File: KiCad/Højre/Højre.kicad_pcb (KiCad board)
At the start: 2 copper layers, 14 parts, among them Q2 NMOS_IRL530, Q4 NMOS_IRL530, Q6 NMOS_IRL530

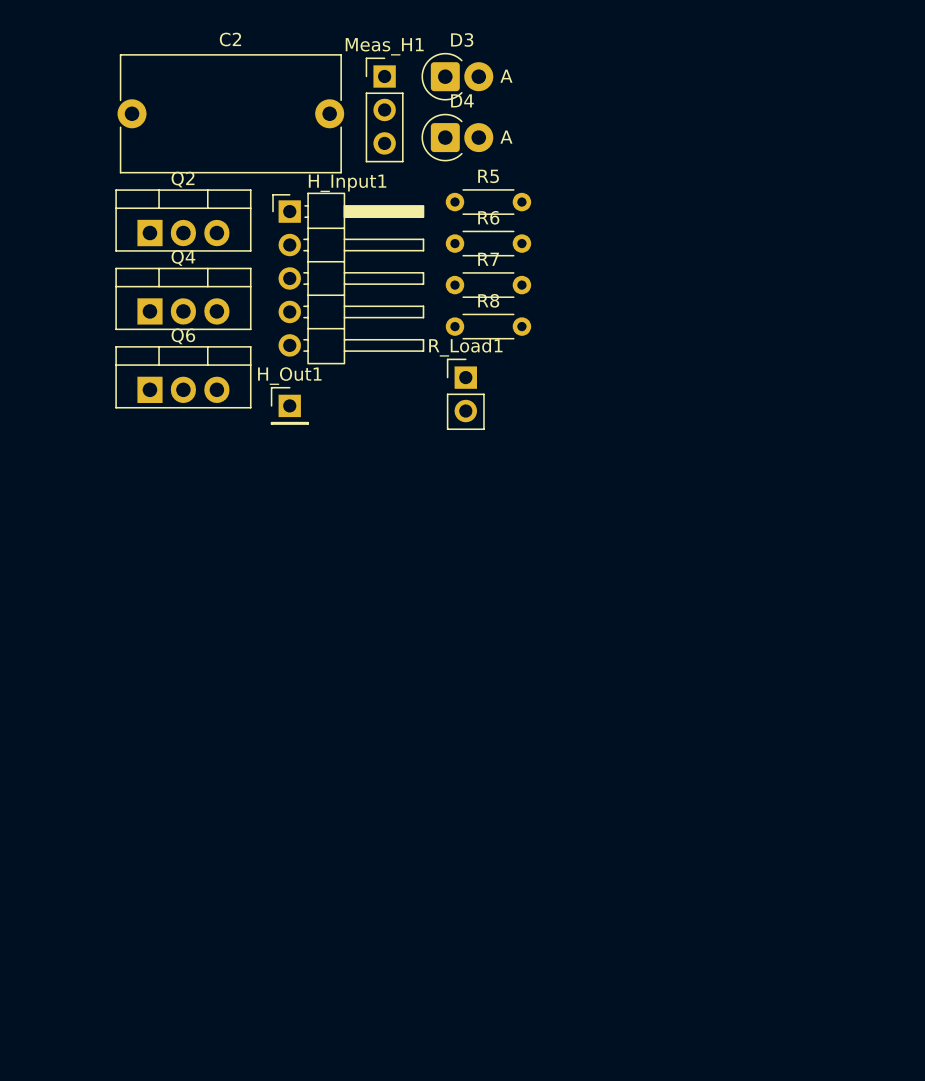
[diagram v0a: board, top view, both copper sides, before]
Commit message: Venstre og Højre pcb klar til produktion
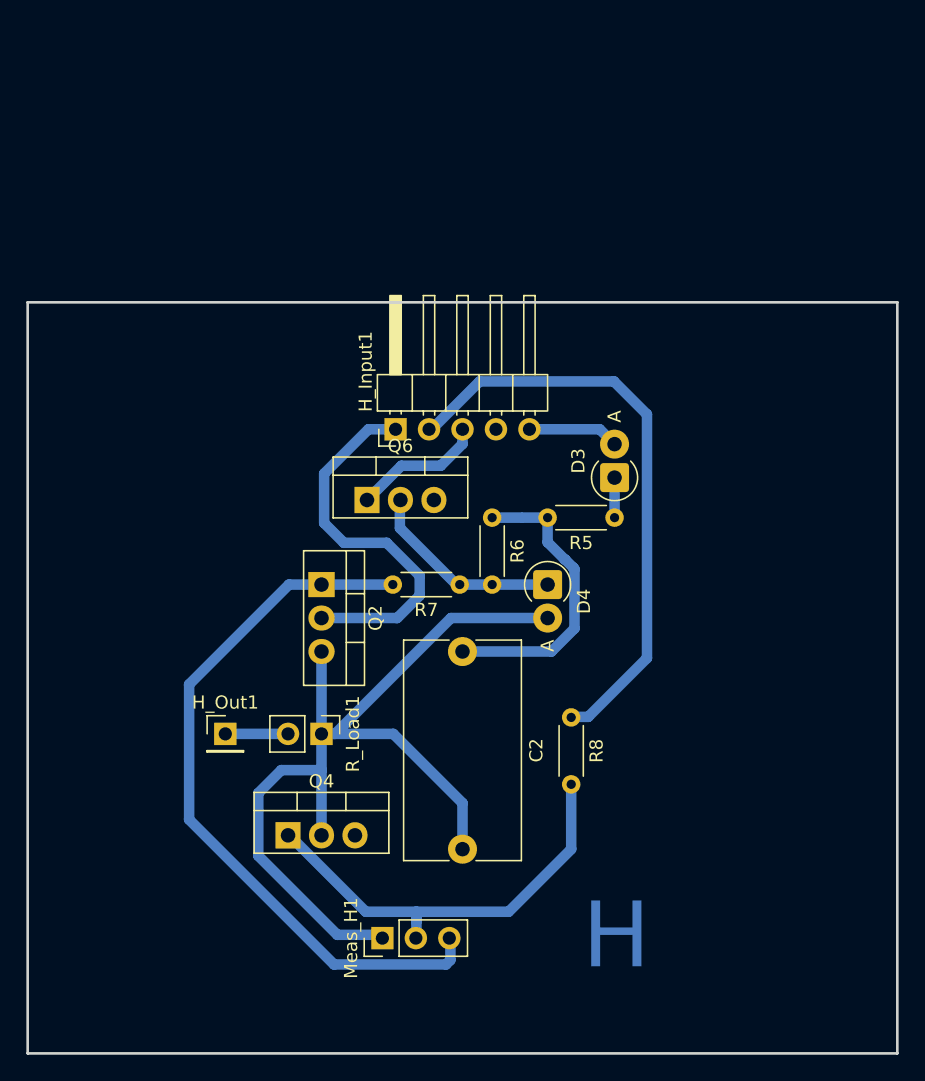
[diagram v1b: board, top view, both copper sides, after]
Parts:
- moved Meas_H1 65.4 mm to (153.4, 134.2), turned to 90 degrees
- moved C2 47.9 mm to (159.5, 112.5), turned to -90 degrees
- moved Q4 41.1 mm to (146.3, 126.5)
- moved D4 34.8 mm to (166.0, 107.4), turned to -90 degrees
- moved D3 33.0 mm to (171.0, 99.3), turned to 90 degrees
- moved R8 30.9 mm to (167.8, 117.5), turned to -90 degrees
- moved Q2 29.7 mm to (148.8, 107.4), turned to -90 degrees
- moved R_Load1 29.2 mm to (148.8, 118.8), turned to -90 degrees
- moved R5 26.8 mm to (171.0, 102.3), turned to 180 degrees
- moved H_Out1 25.4 mm to (141.5, 118.8)
- moved R7 22.7 mm to (159.3, 107.4), turned to 180 degrees
- moved R6 21.0 mm to (161.8, 102.3), turned to -90 degrees
- moved Q6 18.5 mm to (152.2, 101.0)
- moved H_Input1 18.4 mm to (154.4, 95.6), turned to 90 degrees
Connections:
- Q2 pad 1: +9V -> /Meas_GATE_M2
- Q2 pad 2: /Meas_GATE_M2 -> +9V
- Q4 pad 1: /Meas_H_Out -> /Meas_GATE_M4
- Q4 pad 2: /Meas_GATE_M4 -> /Meas_H_Out
- Q6 pad 1: Net-(D4-K) -> /PWM1_NOT
- Q6 pad 2: /PWM1_NOT -> Net-(D4-K)
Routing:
- net /Meas_H_Out: track 0.00 -> 73.3 mm
- net /Meas_GATE_M2: track 0.00 -> 54.8 mm
- net /PWM2: track 0.00 -> 45.2 mm
- net /Meas_GATE_M4: track 0.00 -> 33.4 mm
- net +9V: track 0.00 -> 29.2 mm
- net Net-(C2-Pad1): track 0.00 -> 22.8 mm
- net Net-(D4-K): track 0.00 -> 15.1 mm
- net /PWM1_NOT: track 0.00 -> 10.2 mm
- net +5V: track 0.00 -> 6.93 mm
- net Net-(H_Out1-Pin_1): track 0.00 -> 4.76 mm
- net Net-(D3-K): track 0.00 -> 3.04 mm
- added copper zone on B.Cu, net GND
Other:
- board outline added: 66 x 57 mm
- board text added: "H"
